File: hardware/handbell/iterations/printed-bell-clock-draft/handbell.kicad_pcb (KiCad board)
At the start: 2 copper layers, 44.5 x 48.3 mm, 104 parts, among them IC1 RP2040_QFN56, IC4 LSM6DSOXTR, J1 504050-0291, J2 SM02B-SRSS-TB, Q1 AO3401, Q2 C20917, Q3 DMG3415UFY, Q4 AO3400A, Q5 CSD83325L, U1 W25Q16JVUXIQ TR / 2MB, U2 RT9080-3.3, U3 MCP73831T-2ACI/OT, U4 MAX98357A, U5 TPS61023DRLR, U6 BQ29700DSER, X6 USB Type C, Y1 12MHz/CL10pF

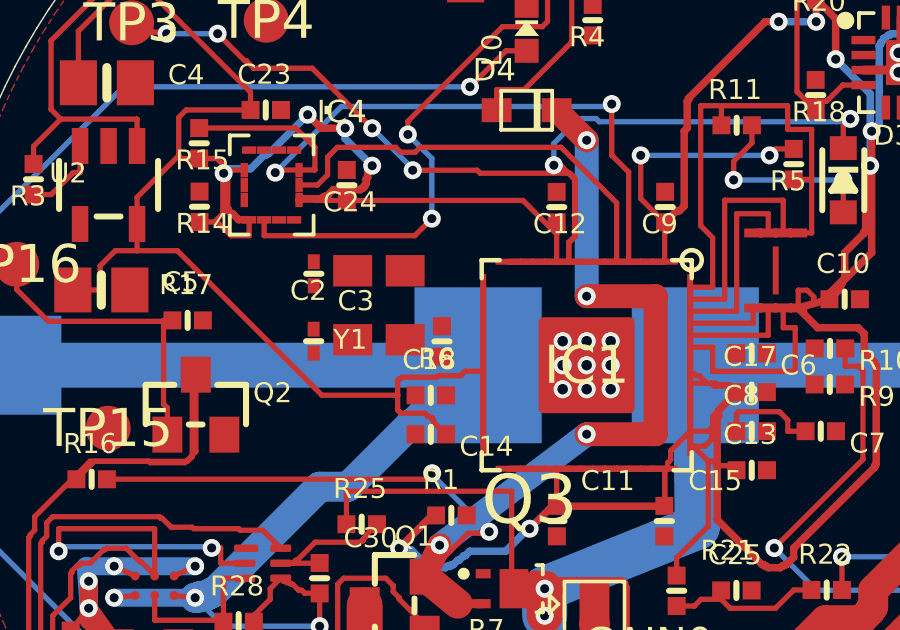
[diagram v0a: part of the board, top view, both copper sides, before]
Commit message: Route first local clock connections with bounded native evidence
Add 15 F-side segments without moves or vias; retain unfinished MCU approaches, final returns and three library mismatch gates.

Co-authored-by: Copilot <223556219+Copilot@users.noreply.github.com>
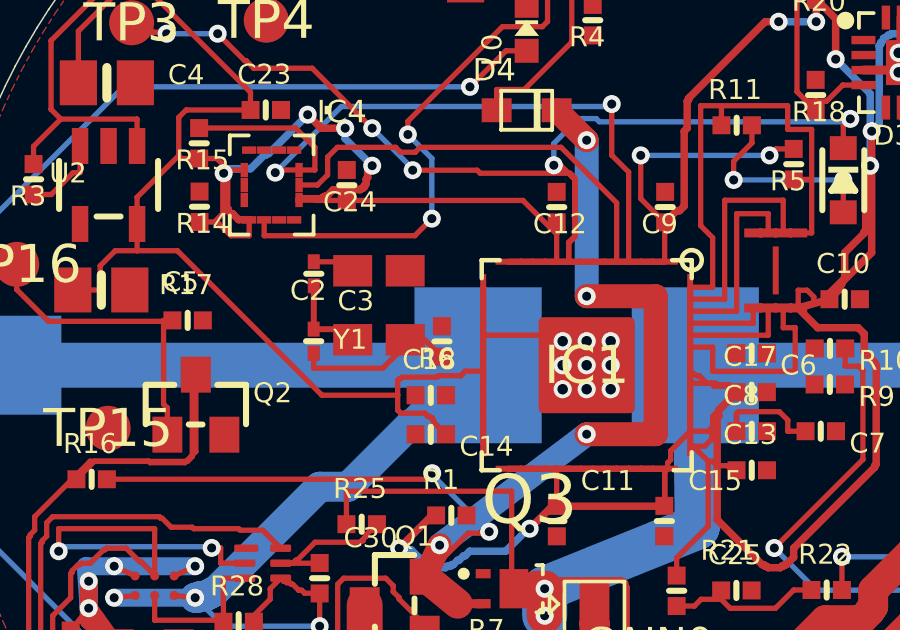
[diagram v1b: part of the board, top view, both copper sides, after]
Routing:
- net GND: track 97.5 -> 104.8 mm
- net Net-(C3-Pad2): track 0.00 -> 5.52 mm
- net Net-(IC1-XIN): track 0.00 -> 1.42 mm
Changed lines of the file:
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@@
 		)
 	)
-)
+(segment (start 90.9036 96.55245) (end 91.899655 96.55245) (width 0.1778) (layer "F.Cu") (net "Net-(IC1-XIN)"))
+(segment (start 91.899655 96.55245) (end 92.199801 96.852596) (width 0.1778) (layer "F.Cu") (net "Net-(IC1-XIN)"))
+(segment (start 90.899181 99.599331) (end 90.899181 100.1) (width 0.1778) (layer "F.Cu") (net "Net-(C3-Pad2)"))
+(segment (start 90.899181 100.1) (end 93.2 100.1) (width 0.1778) (layer "F.Cu") (net "Net-(C3-Pad2)"))
+(segment (start 93.2 100.1) (end 93.949801 99.350199) (width 0.1778) (layer "F.Cu") (net "Net-(C3-Pad2)"))
+(segment (start 93.949801 99.350199) (end 93.949801 99.152596) (width 0.1778) (layer "F.Cu") (net "Net-(C3-Pad2)"))
+(segment (start 93.949801 99.152596) (end 94.6 99.152596) (width 0.1778) (layer "F.Cu") (net "Net-(C3-Pad2)"))
+(segment (start 94.6 99.152596) (end 95.161305 99.713901) (width 0.1778) (layer "F.Cu") (net "Net-(C3-Pad2)"))
+(segment (start 95.161305 99.713901) (end 95.175414 99.713901) (width 0.1778) (layer "F.Cu") (net "Net-(C3-Pad2)"))
+(segment (start 90.9036 97.35245) (end 90.9036 98.794912) (width 0.2) (layer "F.Cu") (net "GND"))
+(segment (start 90.9036 98.794912) (end 90.899181 98.799331) (width 0.2) (layer "F.Cu") (net "GND"))
+(segment (start 90.899181 98.799331) (end 91.846536 98.799331) (width 0.2) (layer "F.Cu") (net "GND"))
+(segment (start 91.846536 98.799331) (end 92.199801 99.152596) (width 0.2) (layer "F.Cu") (net "GND"))
+(segment (start 96.55 99.0) (end 100.0 99.0) (width 0.1778) (layer "F.Cu") (net "GND"))
+(segment (start 100.0 99.0) (end 100.0 100.0) (width 0.1778) (layer "F.Cu") (net "GND")))
